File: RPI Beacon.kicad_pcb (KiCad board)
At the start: 2 copper layers, 75 x 127 mm, 40 parts, among them J1 USB_C_Receptacle_PowerOnly_6P, Q1 FS8205A, SW1 SW_SPDT, U1 MCP73831-2-OT, U2 DW01A

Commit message: Completed more of the PCB Layout work
yes
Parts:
- moved U2 10.7 mm to (132.7, 75.0)
- moved C3 8.92 mm to (139.2, 76.0)
- moved R18 6.15 mm to (128.0, 86.5), turned to 180 degrees
- moved R13 6.10 mm to (93.0, 64.6)
- moved R17 4.47 mm to (123.9, 75.4)
- moved Q1 3.84 mm to (122.0, 82.2), turned to 90 degrees
- moved C2 1.90 mm to (86.7, 87.4), turned to 180 degrees
- moved R14 1.65 mm to (85.6, 71.4), turned to 90 degrees
- moved R3 0.42 mm to (85.5, 156.0), turned to 180 degrees
- moved R7 0.40 mm to (85.6, 95.5)
- moved R2 0.29 mm to (85.5, 133.0), turned to 180 degrees
- moved R8 0.29 mm to (85.6, 121.6)
- moved R9 0.23 mm to (85.5, 144.6)
- turned R1 to 180 degrees
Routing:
- net GND: track 0.00 -> 260.9 mm, vias 0 -> 6
- net Net-(SW1-C): track 0.00 -> 208.0 mm, vias 0 -> 4
- net /BAT-: track 0.00 -> 137.9 mm, vias 0 -> 4
- net /BAT+: track 0.00 -> 55.5 mm
- net /VBUS: track 0.00 -> 51.4 mm, vias 0 -> 6
- net Net-(U2-VCC): track 0.00 -> 25.5 mm, vias 0 -> 2
- net Net-(D13-A): track 0.00 -> 24.0 mm, vias 0 -> 2
- net Net-(U2-CS): track 0.00 -> 14.2 mm
- net Net-(U2-OD): track 0.00 -> 14.1 mm
- net Net-(U1-PROG): track 0.00 -> 10.8 mm
- net Net-(U2-OC): track 0.00 -> 10.8 mm, vias 0 -> 2
- net Net-(U1-STAT): track 0.00 -> 7.64 mm
- net Net-(J1-CC1): track 0.00 -> 6.76 mm, vias 0 -> 1
- net Net-(J1-CC2): track 0.00 -> 6.51 mm, vias 0 -> 1
- net Net-(D7-A): track 0.00 -> 5.65 mm
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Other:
- board text added: "Navigational Beacon PCB Made possible by RPI & Mercer X Labs Designed by Andrew Dieu"

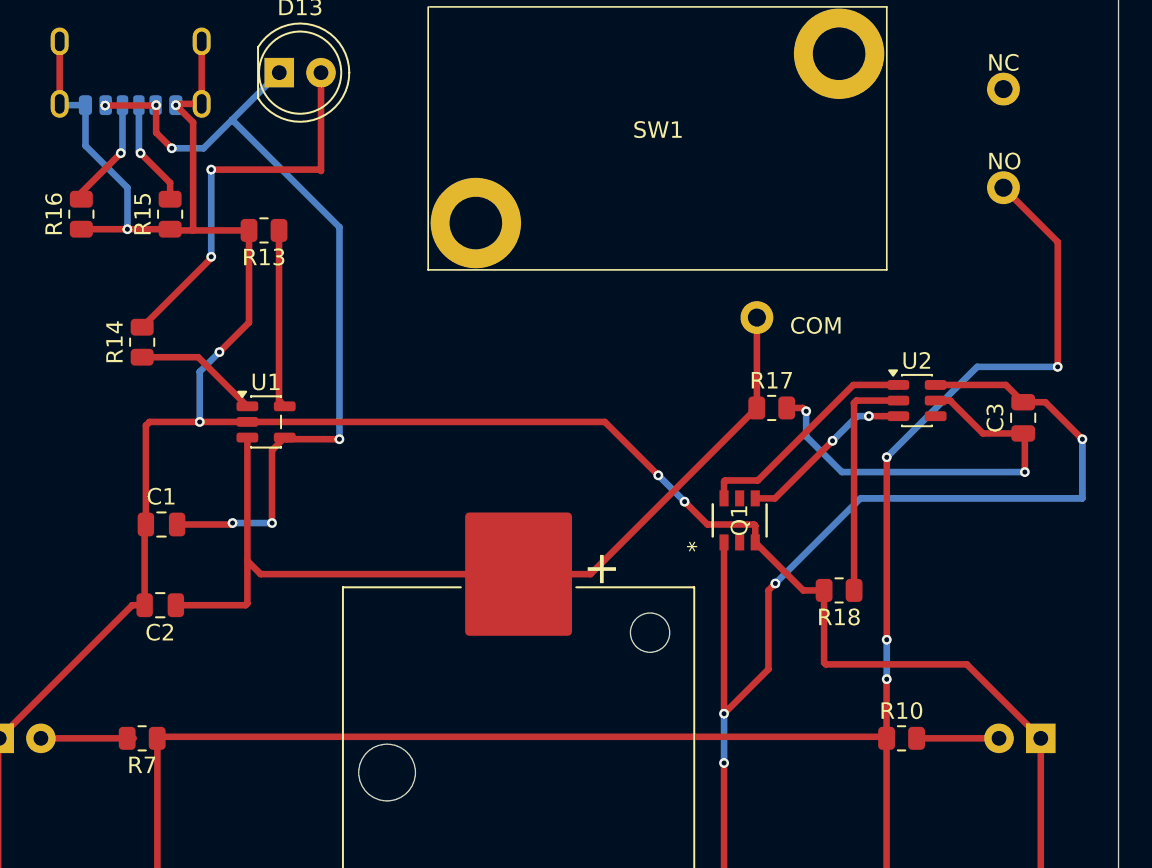
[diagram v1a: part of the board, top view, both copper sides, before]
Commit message: Added V1 Gerbers
Finally. Time to start prototyping!
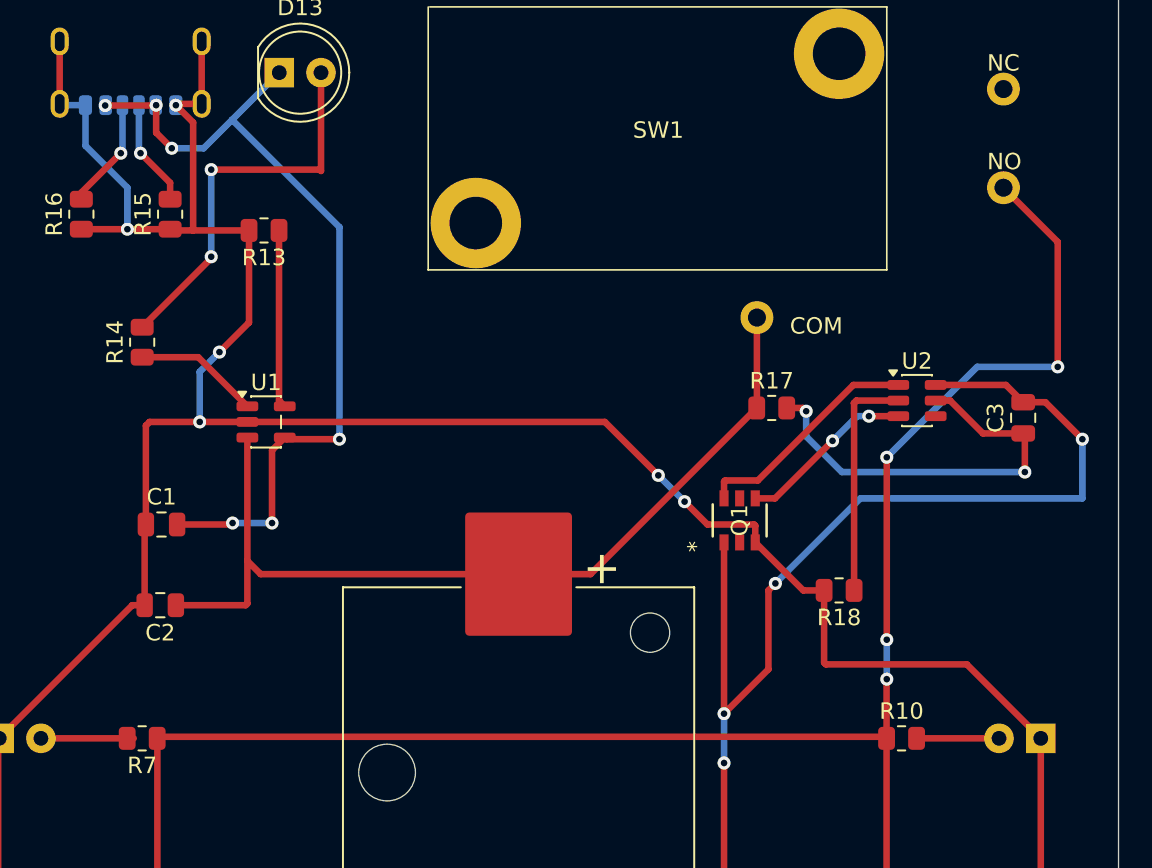
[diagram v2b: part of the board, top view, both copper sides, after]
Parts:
- added G***: LOGO, LOGO, B.Cu at (106.7, 112.7)
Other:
- board text added: "Navigational Beacon PCB Made possible by RPI & Mercer X Labs Designed by Andrew Dieu Version 1"
- board text removed: "Navigational Beacon PCB Made possible by RPI & Mercer X Labs Designed by Andrew Dieu"

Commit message: minor revisions
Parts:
- moved C3 32.1 mm to (160.9, 52.3)
- moved D11 32.1 mm to (161.9, 97.8)
- moved R11 32.1 mm to (153.7, 97.8)
- moved R12 32.1 mm to (153.8, 120.7)
- moved C2 32.1 mm to (108.4, 63.7)
- moved D2 32.1 mm to (98.2, 109.3)
- moved Q1 32.1 mm to (143.7, 58.5)
- moved R14 32.1 mm to (107.3, 47.7)
- moved R2 32.1 mm to (107.2, 109.3)
- moved R7 32.1 mm to (107.3, 71.8)
- moved U1 32.1 mm to (114.8, 52.5)
- moved D13 32.1 mm to (115.6, 31.3)
- moved D3 32.1 mm to (98.2, 132.3)
- moved D6 32.1 mm to (161.8, 132.5)
- moved D8 32.1 mm to (98.3, 97.9)
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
